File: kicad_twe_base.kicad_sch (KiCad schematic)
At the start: 9 parts, among them J1 Conn_01x14, J2 Conn_01x14, J3 Conn_01x07, SW1 SW_SPDT, SW2 SW_Push, SW3 SW_SPDT, U1 BHC-CR123A, U2 TWE-L-DP-W

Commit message: 123Aのバッテリーホルダを追加
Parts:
- removed U1: BHC-CR123A, BHC-CR123A, symbol BHC-CR123A:BHC-CR123A
- added U1: BHC-CR123A, KICAD_MYLIB:BHC-CR123A, symbol KICAD_MYLIB:BHC-CR123A
- JP1: footprint (none) -> Jumper:SolderJumper-3_P1.3mm_Open_RoundedPad1.0x1.5mm_NumberLabels
- SW1, SW3: footprint (none) -> KICAD_MYLIB:SW_SLIDE_sengoku
- SW2: footprint (none) -> KICAD_MYLIB:SW_PUSH_2pin
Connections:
- net at J1.1 (Pin_1), J1.14 (Pin_14), J3.1 (Pin_1)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: now also U1.2 (-)
- net at JP1.3 (B), SW3.1 (A): now also U1.1 (+)
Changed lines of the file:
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@@
     (stroke (width 0) (type default) (color 0 0 0 0))
   )
-  (wire (pts (xy 76.2 91.44) (xy 76.2 116.84))
+  (wire (pts (xy 76.2 88.9) (xy 76.2 116.84))
     (stroke (width 0) (type default) (color 0 0 0 0))
   )
@@
     (stroke (width 0) (type default) (color 0 0 0 0))
   )
-  (wire (pts (xy 76.2 71.12) (xy 76.2 36.83))
+  (wire (pts (xy 76.2 36.83) (xy 76.2 73.66))
     (stroke (width 0) (type default) (color 0 0 0 0))
   )
@@
     (property "Reference" "SW1" (id 0) (at 247.65 63.5 0))
     (property "Value" "SW_SPDT" (id 1) (at 247.65 66.04 0))
-    (property "Footprint" "" (id 2) (at 247.65 71.12 0)
+    (property "Footprint" "KICAD_MYLIB:SW_SLIDE_sengoku" (id 2) (at 247.65 71.12 0)
       (effects (font (size 1.27 1.27)) hide)
     )
@@
       (effects (font (size 1.27 1.27)) (justify right))
     )
-    (property "Footprint" "" (id 2) (at 203.2 48.26 0)
+    (property "Footprint" "KICAD_MYLIB:SW_SLIDE_sengoku" (id 2) (at 203.2 48.26 0)
       (effects (font (size 1.27 1.27)) hide)
     )
@@
     (property "Reference" "JP1" (id 0) (at 203.2 30.48 0))
     (property "Value" "SolderJumper_3_Open" (id 1) (at 203.2 33.02 0))
-    (property "Footprint" "" (id 2) (at 203.2 36.83 0)
+    (property "Footprint" "Jumper:SolderJumper-3_P1.3mm_Open_RoundedPad1.0x1.5mm_NumberLabels" (id 2) (at 203.2 36.83 0)
       (effects (font (size 1.27 1.27)) hide)
     )
@@
     (pin "7")
   )
-  (symbol (lib_id "BHC-CR123A:BHC-CR123A") (at 76.2 71.12 270) (unit 1)
-    (in_bom yes) (on_board yes) (fields_autoplaced)
-    (property "Reference" "U1" (id 0) (at 72.39 62.2301 90)
-      (effects (font (size 1.27 1.27)) (justify left))
-    )
-    (property "Value" "BHC-CR123A" (id 1) (at 72.39 59.6901 90)
-      (effects (font (size 1.27 1.27)) (justify left))
-    )
-    (property "Footprint" "BHC-CR123A" (id 2) (at 73.66 54.61 0)
-      (effects (font (size 1.27 1.27)) (justify left) hide)
-    )
-    (property "Datasheet" "http://www.farnell.com/cad/1868607.pdf" (id 3) (at 68.58 54.61 0)
-      (effects (font (size 1.27 1.27)) (justify left) hide)
-    )
-    (property "Description" "PRO POWER - BHC-CR123A - BATTERY HOLDER, CR123A, PCB" (id 4) (at 78.74 54.61 0)
-      (effects (font (size 1.27 1.27)) (justify left) hide)
-    )
-    (property "Height" "" (id 5) (at 81.28 54.61 0)
-      (effects (font (size 1.27 1.27)) (justify left) hide)
-    )
-    (property "Manufacturer_Name" "PRO POWER" (id 6) (at 83.82 54.61 0)
-      (effects (font (size 1.27 1.27)) (justify left) hide)
-    )
-    (property "Manufacturer_Part_Number" "BHC-CR123A" (id 7) (at 86.36 54.61 0)
-      (effects (font (size 1.27 1.27)) (justify left) hide)
-    )
-    (property "Mouser Part Number" "" (id 8) (at 88.9 54.61 0)
-      (effects (font (size 1.27 1.27)) (justify left) hide)
-    )
-    (property "Mouser Price/Stock" "" (id 9) (at 91.44 54.61 0)
-      (effects (font (size 1.27 1.27)) (justify left) hide)
-    )
-    (property "RS Part Number" "" (id 10) (at 93.98 54.61 0)
-      (effects (font (size 1.27 1.27)) (justify left) hide)
-    )
-    (property "RS Price/Stock" "" (id 11) (at 96.52 54.61 0)
-      (effects (font (size 1.27 1.27)) (justify left) hide)
+  (symbol (lib_id "KICAD_MYLIB:BHC-CR123A") (at 73.66 91.44 0) (unit 1)
+    (in_bom yes) (on_board yes) (fields_autoplaced)
+    (property "Reference" "U1" (id 0) (at 82.55 76.1999 0)
+      (effects (font (size 1.27 1.27)) (justify left))
+    )
+    (property "Value" "BHC-CR123A" (id 1) (at 82.55 78.7399 0)
+      (effects (font (size 1.27 1.27)) (justify left))
+    )
+    (property "Footprint" "KICAD_MYLIB:BHC-CR123A" (id 2) (at 67.31 88.9 0)
+      (effects (font (size 1.27 1.27)) hide)
+    )
+    (property "Datasheet" "" (id 3) (at 67.31 88.9 0)
+      (effects (font (size 1.27 1.27)) hide)
     )
     (pin "1")
@@
     (property "Reference" "SW2" (id 0) (at 247.65 54.61 0))
     (property "Value" "SW_Push" (id 1) (at 247.65 57.15 0))
-    (property "Footprint" "" (id 2) (at 247.65 57.15 0)
+    (property "Footprint" "KICAD_MYLIB:SW_PUSH_2pin" (id 2) (at 247.65 57.15 0)
       (effects (font (size 1.27 1.27)) hide)
     )
@@
     )
     (path "/5aecb719-693d-4423-ab6c-cad7b519f566"
-      (reference "JP1") (unit 1) (value "SolderJumper_3_Open") (footprint "")
+      (reference "JP1") (unit 1) (value "SolderJumper_3_Open") (footprint "Jumper:SolderJumper-3_P1.3mm_Open_RoundedPad1.0x1.5mm_NumberLabels")
     )
     (path "/0ba70209-97c8-424e-ab67-ae21eacb2df5"
-      (reference "SW1") (unit 1) (value "SW_SPDT") (footprint "")
+      (reference "SW1") (unit 1) (value "SW_SPDT") (footprint "KICAD_MYLIB:SW_SLIDE_sengoku")
     )
     (path "/b76b6acd-99e4-45ab-9f46-b307d4413f10"
-      (reference "SW2") (unit 1) (value "SW_Push") (footprint "")
+      (reference "SW2") (unit 1) (value "SW_Push") (footprint "KICAD_MYLIB:SW_PUSH_2pin")
     )
     (path "/39f8da0b-9b8e-4f9e-871d-7225e4b56a49"
-      (reference "SW3") (unit 1) (value "SW_SPDT") (footprint "")
-    )
-    (path "/895cd017-6c6b-4a20-bb97-692eedc2704f"
-      (reference "U1") (unit 1) (value "BHC-CR123A") (footprint "BHC-CR123A")
+      (reference "SW3") (unit 1) (value "SW_SPDT") (footprint "KICAD_MYLIB:SW_SLIDE_sengoku")
+    )
+    (path "/a9c7df09-2ae6-42c3-b8f6-c45c99a2b319"
+      (reference "U1") (unit 1) (value "BHC-CR123A") (footprint "KICAD_MYLIB:BHC-CR123A")
     )
     (path "/1a0d41cc-b690-4174-ae65-31ff33a86aac"

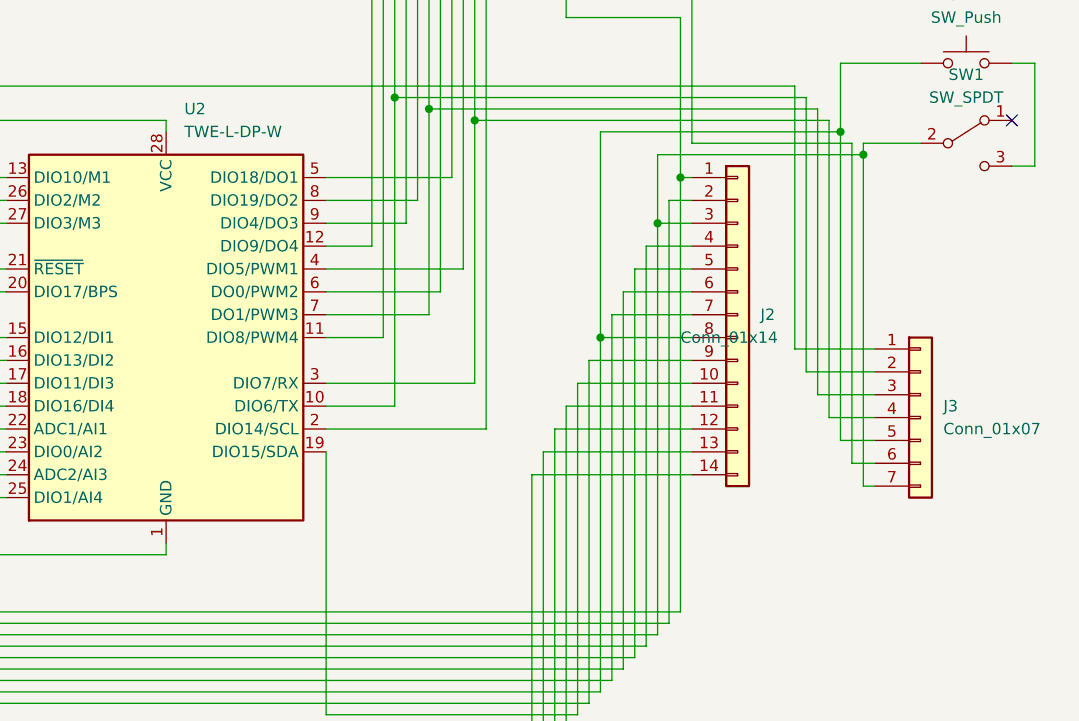
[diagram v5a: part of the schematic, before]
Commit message: リセットSWとPRG SWをGNDに落とし忘れていた
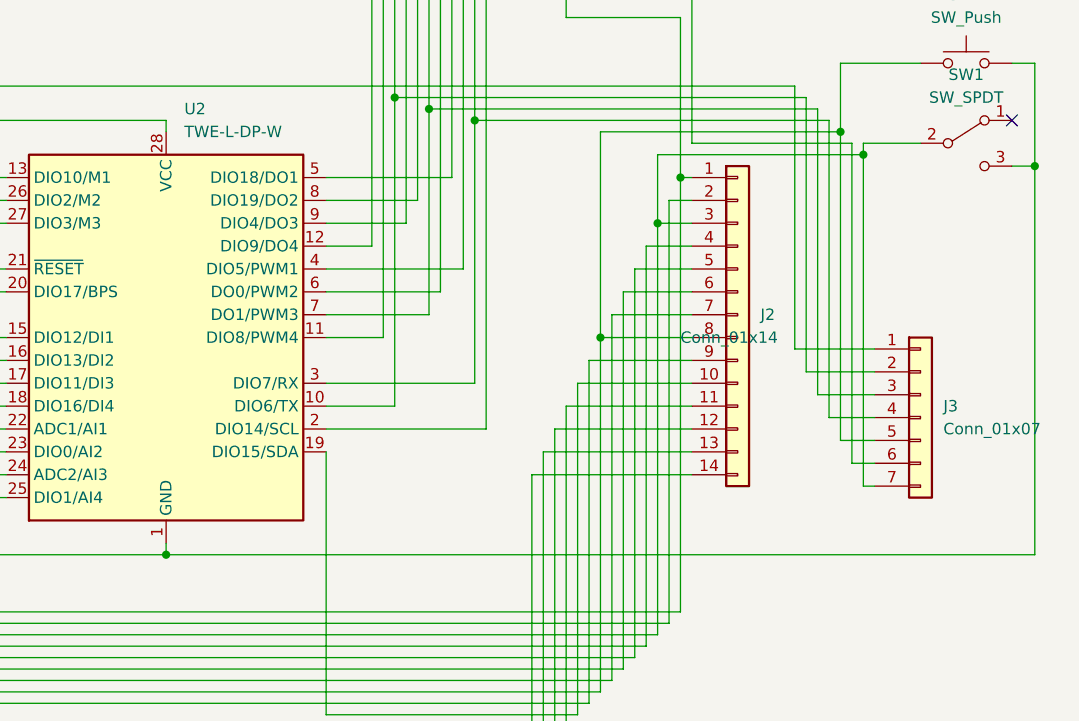
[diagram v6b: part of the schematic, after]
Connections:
- net at SW1.3 (C), SW2.2: now also J1.1 (Pin_1), J1.14 (Pin_14), J3.1 (Pin_1), U1.2 (-), U2.1 (GND), U2.14 (GND)
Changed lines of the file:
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@@
   (junction (at 207.01 92.71) (diameter 0) (color 0 0 0 0)
+  )
+  (junction (at 255.27 73.66) (diameter 0) (color 0 0 0 0)
+  )
+  (junction (at 158.75 116.84) (diameter 0) (color 0 0 0 0)
   )
   (junction (at 217.17 41.91) (diameter 0) (color 0 0 0 0)
@@
   )
   (wire (pts (xy 217.17 36.83) (xy 217.17 41.91))
+    (stroke (width 0) (type default) (color 0 0 0 0))
+  )
+  (wire (pts (xy 255.27 116.84) (xy 255.27 73.66))
     (stroke (width 0) (type default) (color 0 0 0 0))
   )
@@
     (stroke (width 0) (type default) (color 0 0 0 0))
   )
+  (wire (pts (xy 158.75 116.84) (xy 255.27 116.84))
+    (stroke (width 0) (type default) (color 0 0 0 0))
+  )

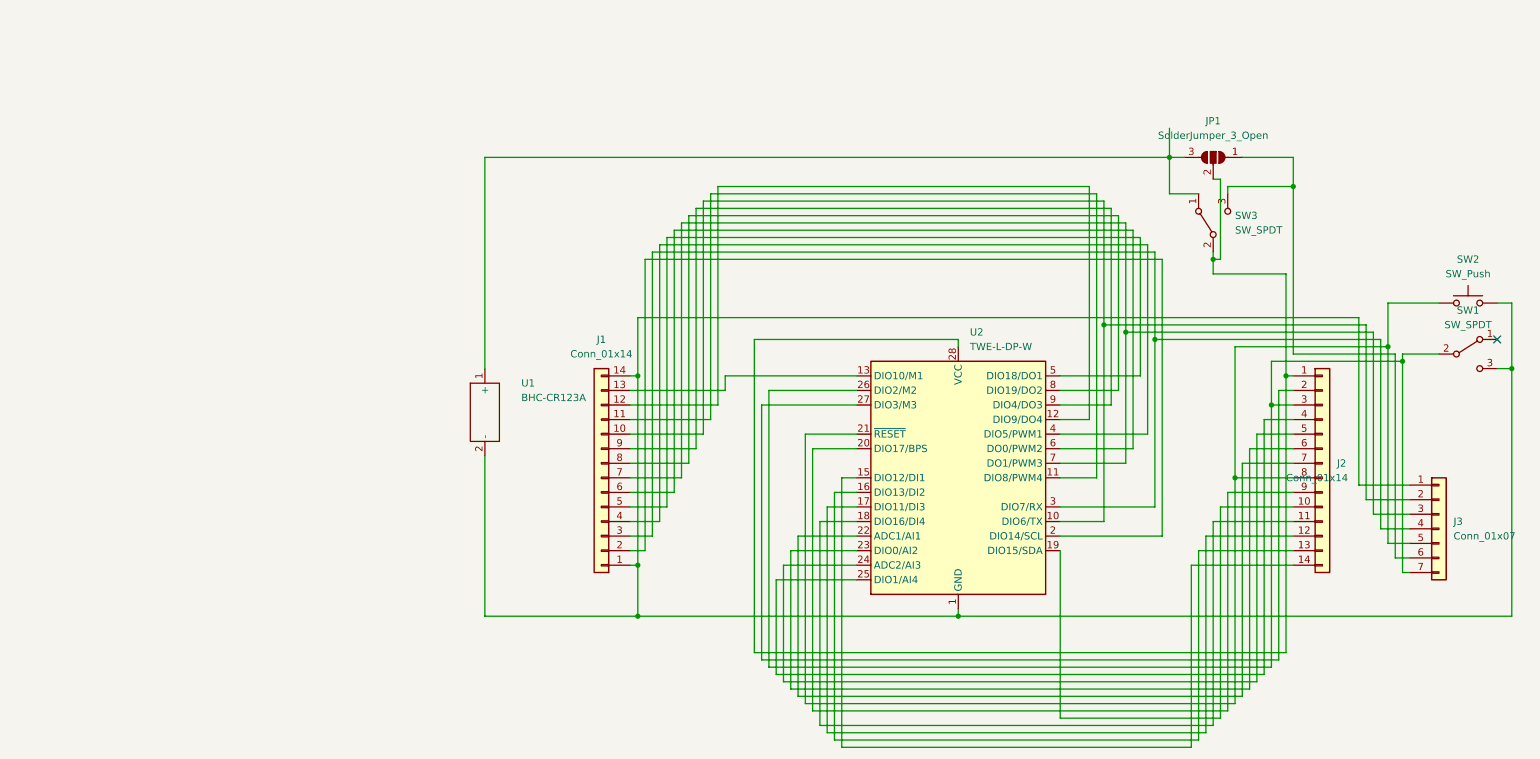
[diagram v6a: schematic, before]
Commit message: VCCとGNDのPWR_FLAGをつけた
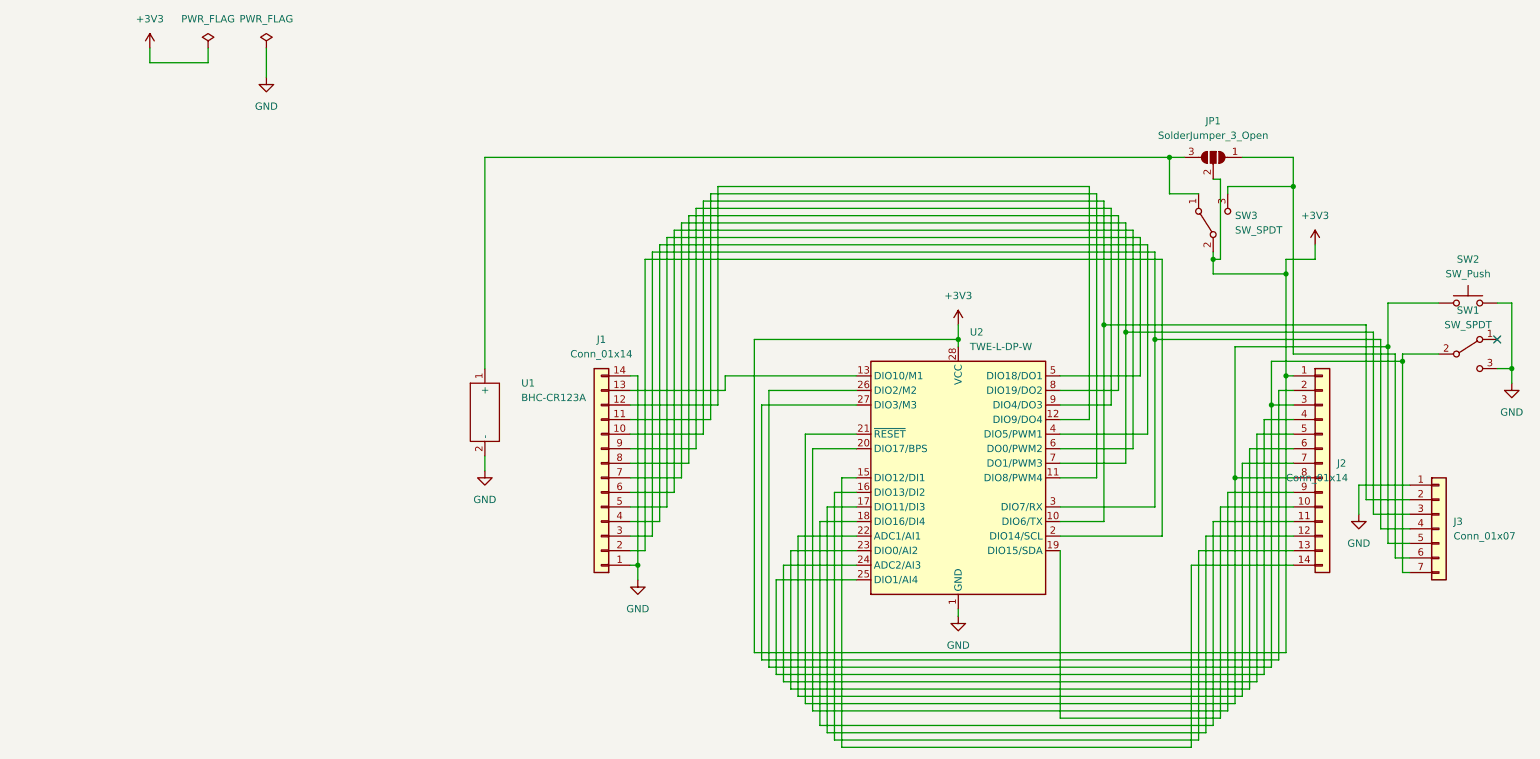
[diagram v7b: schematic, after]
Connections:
- net GND: now reaches J1.1 (Pin_1), J1.14 (Pin_14), J3.1 (Pin_1), SW1.3 (C), SW2.2, U1.2 (-), U2.1 (GND), U2.14 (GND)
- net +3V3: now reaches J2.1 (Pin_1), JP1.2 (C), SW3.2 (B), U2.28 (VCC)
